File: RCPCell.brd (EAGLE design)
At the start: 94.7 x 44.5 mm, 28 parts, among them U1 PESDXS4UD, U7 FAN8303

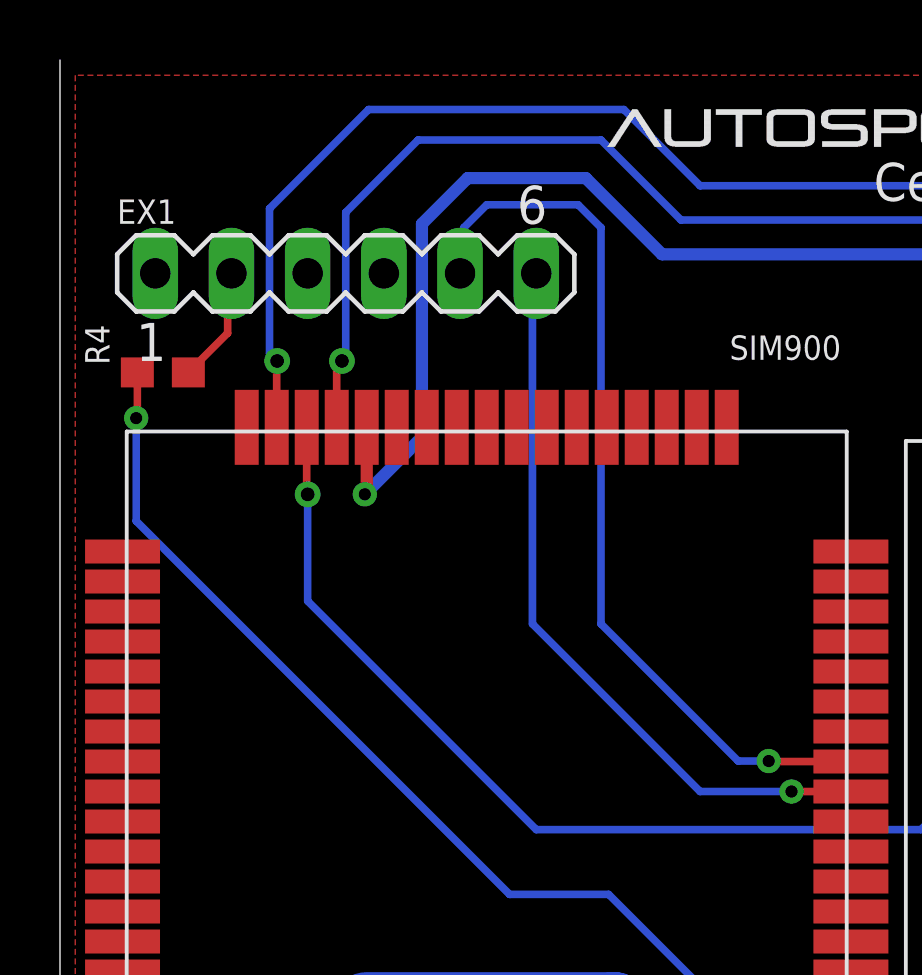
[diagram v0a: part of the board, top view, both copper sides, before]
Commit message: fixed flipped routing on I/O header
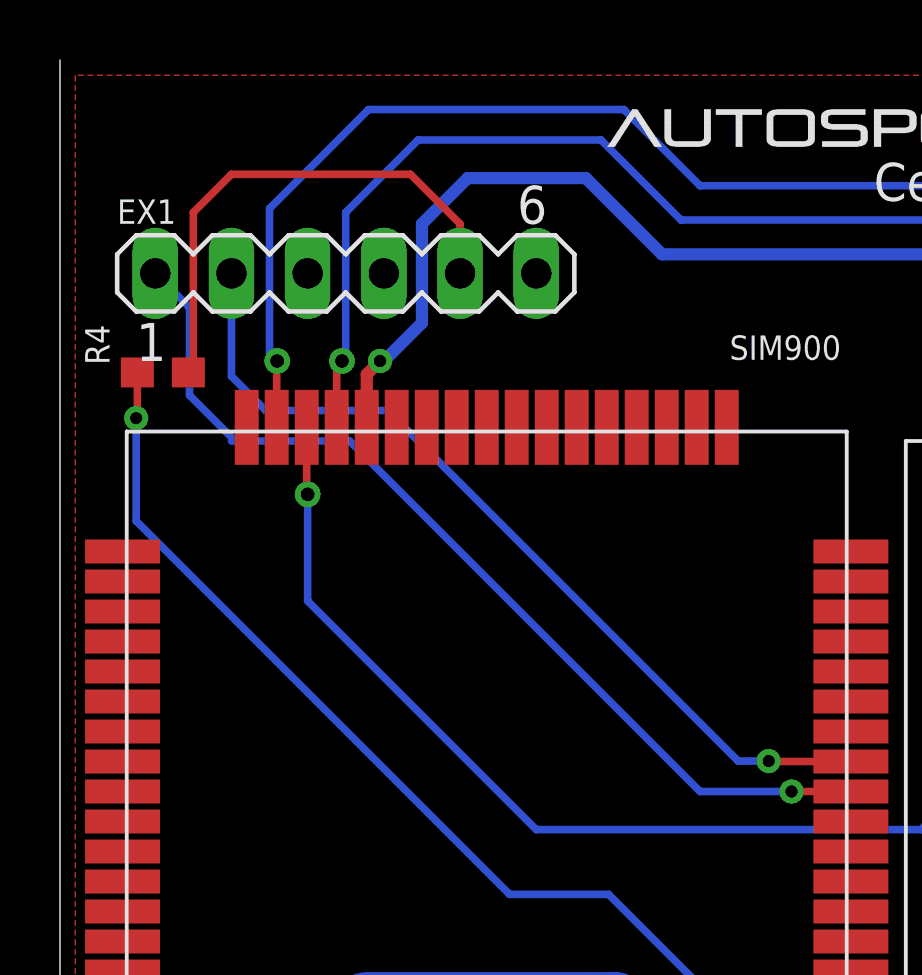
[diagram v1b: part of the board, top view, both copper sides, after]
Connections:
- net DIN: now also EX1.2; no longer EX1.5
- net DOUT: now also EX1.1; no longer EX1.6
- net EXT_CTRL: now also EX1.5; no longer EX1.2
- net GND: now also EX1.6; no longer EX1.1
- net USB_DM_HS_OUT: now also EX1.4; no longer EX1.3
- net USB_DP_HS_OUT: now also EX1.3; no longer EX1.4
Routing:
- net EXT_CTRL: track 3.90 -> 17.3 mm
- net DOUT: track 24.7 -> 32.2 mm
- net SIM_VDD: track 54.5 -> 50.1 mm
- net DIN: track 30.2 -> 29.4 mm
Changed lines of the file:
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@@
 <setting verticaltext="up"/>
 </settings>
-<grid distance="0.05" unitdist="inch" unit="inch" style="lines" multiple="1" display="no" altdistance="0.01" altunitdist="inch" altunit="inch"/>
+<grid distance="0.005" unitdist="inch" unit="inch" style="lines" multiple="1" display="no" altdistance="0.01" altunitdist="inch" altunit="inch"/>
 <layers>
 <layer number="1" name="Top" color="4" fill="1" visible="yes" active="yes"/>
@@
 <signal name="DIN">
 <contactref element="SIM900" pad="10"/>
-<contactref element="EX1" pad="5"/>
-<wire x1="15.875" y1="37.338" x2="16.002" y2="37.465" width="0.254" layer="16"/>
-<wire x1="16.002" y1="37.465" x2="16.002" y2="38.862" width="0.254" layer="16"/>
-<wire x1="16.002" y1="38.862" x2="16.764" y2="39.624" width="0.254" layer="16"/>
-<wire x1="16.764" y1="39.624" x2="19.812" y2="39.624" width="0.254" layer="16"/>
-<wire x1="19.812" y1="39.624" x2="20.574" y2="38.862" width="0.254" layer="16"/>
-<wire x1="20.574" y1="38.862" x2="20.574" y2="25.654" width="0.254" layer="16"/>
-<wire x1="20.574" y1="25.654" x2="25.146" y2="21.082" width="0.254" layer="16"/>
 <wire x1="25.146" y1="21.082" x2="26.162" y2="21.082" width="0.254" layer="16"/>
 <via x="26.162" y="21.082" extent="1-16" drill="0.4064"/>
 <wire x1="26.162" y1="21.082" x2="26.178" y2="21.066" width="0.254" layer="1"/>
 <wire x1="26.178" y1="21.066" x2="28.903" y2="21.066" width="0.254" layer="1"/>
+<contactref element="EX1" pad="2"/>
+<wire x1="8.255" y1="33.909" x2="8.255" y2="37.338" width="0.254" layer="16"/>
+<wire x1="25.146" y1="21.082" x2="13.462" y2="32.766" width="0.254" layer="16"/>
+<wire x1="13.462" y1="32.766" x2="9.398" y2="32.766" width="0.254" layer="16"/>
+<wire x1="9.398" y1="32.766" x2="8.255" y2="33.909" width="0.254" layer="16"/>
 </signal>
 <signal name="DOUT">
 <contactref element="SIM900" pad="9"/>
-<contactref element="EX1" pad="6"/>
-<wire x1="18.415" y1="37.338" x2="18.288" y2="37.211" width="0.254" layer="16"/>
-<wire x1="18.288" y1="37.211" x2="18.288" y2="25.654" width="0.254" layer="16"/>
-<wire x1="18.288" y1="25.654" x2="23.876" y2="20.066" width="0.254" layer="16"/>
 <wire x1="23.876" y1="20.066" x2="26.924" y2="20.066" width="0.254" layer="16"/>
 <via x="26.924" y="20.066" extent="1-16" drill="0.4064"/>
 <wire x1="26.924" y1="20.066" x2="28.903" y2="20.066" width="0.254" layer="1"/>
+<contactref element="EX1" pad="1"/>
+<wire x1="5.715" y1="37.338" x2="6.858" y2="36.195" width="0.254" layer="16"/>
+<wire x1="23.876" y1="20.066" x2="12.192" y2="31.75" width="0.254" layer="16"/>
+<wire x1="12.192" y1="31.75" x2="8.382" y2="31.75" width="0.254" layer="16"/>
+<wire x1="8.382" y1="31.75" x2="8.255" y2="31.75" width="0.254" layer="16"/>
+<wire x1="6.858" y1="36.195" x2="6.858" y2="33.274" width="0.254" layer="16"/>
+<wire x1="6.858" y1="33.274" x2="8.382" y2="31.75" width="0.254" layer="16"/>
 </signal>
 <signal name="V+">
@@
 <wire x1="41.713" y1="30.791" x2="40.894" y2="29.972" width="0.4064" layer="1"/>
 <wire x1="40.894" y1="29.972" x2="40.894" y2="27.31" width="0.4064" layer="1"/>
-<wire x1="12.764" y1="32.205" x2="12.764" y2="30.036" width="0.4064" layer="1"/>
-<wire x1="12.764" y1="30.036" x2="12.7" y2="29.972" width="0.254" layer="1"/>
-<via x="12.7" y="29.972" extent="1-16" drill="0.4064"/>
-<wire x1="12.7" y1="29.972" x2="14.605" y2="31.877" width="0.4064" layer="16"/>
-<wire x1="14.605" y1="31.877" x2="14.605" y2="38.989" width="0.4064" layer="16"/>
+<via x="13.208" y="34.417" extent="1-16" drill="0.4064"/>
+<wire x1="14.605" y1="35.687" x2="14.605" y2="38.989" width="0.4064" layer="16"/>
 <wire x1="14.605" y1="38.989" x2="16.129" y2="40.513" width="0.4064" layer="16"/>
 <wire x1="16.129" y1="40.513" x2="20.066" y2="40.513" width="0.4064" layer="16"/>
@@
 <wire x1="40.64" y1="32.131" x2="41.468" y2="32.959" width="0.4064" layer="1"/>
 <wire x1="41.468" y1="32.959" x2="41.713" y2="32.959" width="0.254" layer="1"/>
+<wire x1="14.605" y1="35.687" x2="13.335" y2="34.417" width="0.4064" layer="16"/>
+<wire x1="13.335" y1="34.417" x2="13.208" y2="34.417" width="0.4064" layer="16"/>
+<wire x1="12.764" y1="32.205" x2="12.764" y2="33.973" width="0.4064" layer="1"/>
+<wire x1="12.764" y1="33.973" x2="13.208" y2="34.417" width="0.4064" layer="1"/>
 </signal>
 <signal name="SIM_DATA">
@@
 <wire x1="83.152" y1="30.955" x2="83.058" y2="30.861" width="1.6764" layer="1"/>
 </signal>
-<signal name="USB_DM_HS_OUT">
-<contactref element="EX1" pad="3"/>
-</signal>
-<signal name="USB_DP_HS_OUT">
-<contactref element="EX1" pad="4"/>
-</signal>
 <signal name="N$1">
 <contactref element="R8" pad="2"/>
@@
 </signal>
 <signal name="EXT_CTRL">
-<contactref element="EX1" pad="2"/>
 <contactref element="R4" pad="2"/>
-<wire x1="8.255" y1="37.338" x2="8.128" y2="37.211" width="0.254" layer="1"/>
-<wire x1="8.128" y1="37.211" x2="8.128" y2="35.345" width="0.254" layer="1"/>
-<wire x1="8.128" y1="35.345" x2="6.819" y2="34.036" width="0.254" layer="1"/>
+<contactref element="EX1" pad="5"/>
+<wire x1="6.819" y1="34.036" x2="6.985" y2="34.036" width="0.254" layer="1"/>
+<wire x1="6.985" y1="34.036" x2="6.985" y2="39.37" width="0.254" layer="1"/>
+<wire x1="6.985" y1="39.37" x2="8.255" y2="40.64" width="0.254" layer="1"/>
+<wire x1="8.255" y1="40.64" x2="14.224" y2="40.64" width="0.254" layer="1"/>
+<wire x1="14.224" y1="40.64" x2="15.875" y2="38.989" width="0.254" layer="1"/>
+<wire x1="15.875" y1="38.989" x2="15.875" y2="37.338" width="0.254" layer="1"/>
 </signal>
 <signal name="GND">
@@
 <contactref element="U1" pad="5"/>
 <contactref element="U1" pad="2"/>
-<contactref element="EX1" pad="1"/>
 <contactref element="EX2" pad="1"/>
 <contactref element="EX2" pad="2"/>
@@
 <wire x1="19.304" y1="5.842" x2="19.304" y2="8.128" width="0.6096" layer="1"/>
 <contactref element="C43" pad="-"/>
+<contactref element="EX1" pad="6"/>
 <wire x1="19.304" y1="3.8481" x2="19.304" y2="3.8481" width="0" layer="19" extent="1-16"/>
 <wire x1="14.224" y1="3.8481" x2="14.224" y2="3.8481" width="0" layer="19" extent="1-16"/>
 </signal>
+<signal name="USB_DM_HS_OUT">
+<contactref element="EX1" pad="4"/>
+</signal>
+<signal name="USB_DP_HS_OUT">
+<contactref element="EX1" pad="3"/>
+</signal>
 </signals>
